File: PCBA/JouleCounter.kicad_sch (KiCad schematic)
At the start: 0 parts

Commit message: Scratching out schematic
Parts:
- added J? (x2): USB_C_Receptacle_USB2.0, symbol Connector:USB_C_Receptacle_USB2.0
- added R?: ?, symbol Device:R_Shunt
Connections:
- new net: J?.A4 (VBUS), J?.A9 (VBUS), J?.B4 (VBUS), J?.B9 (VBUS), R?.4
- new net: J?.A8 (SBU1), J?.A8 (SBU1)
- new net: J?.B8 (SBU2), J?.B8 (SBU2)
- new net CC1: J?.A5 (CC1), J?.A5 (CC1)
- new net CC2: J?.B5 (CC2), J?.B5 (CC2)
- new net GND: J?.A1 (GND), J?.A1 (GND), J?.A12 (GND), J?.A12 (GND), J?.B1 (GND), J?.B1 (GND), J?.B12 (GND), J?.B12 (GND), J?.S1 (SHIELD), J?.S1 (SHIELD)
- new net USB_D+: J?.A6 (D+), J?.A6 (D+), J?.B6 (D+), J?.B6 (D+)
- new net USB_D-: J?.A7 (D-), J?.A7 (D-), J?.B7 (D-), J?.B7 (D-)
- new net VBUS: J?.A4 (VBUS), J?.A9 (VBUS), J?.B4 (VBUS), J?.B9 (VBUS), R?.1
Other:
- removed sheet PineNut-12S
- added sheet FUSB302 (fusb302.kicad_sch)
- added sheet Flash (Flash.kicad_sch)
- added sheet Main MCU (mcu.kicad_sch)
- note added: "Pull high for prog"
- note added: "https://raw.githubusercontent.com/riscv/riscv-debug-spec/master/riscv-debug-stable.pdf Page 92"

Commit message: Input/output jacks
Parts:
- removed J? (x2): USB_C_Receptacle_USB2.0, symbol Connector:USB_C_Receptacle_USB2.0
- removed R?: ?, symbol Device:R_Shunt
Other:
- added sheet Measurement ports (measurement.kicad_sch)

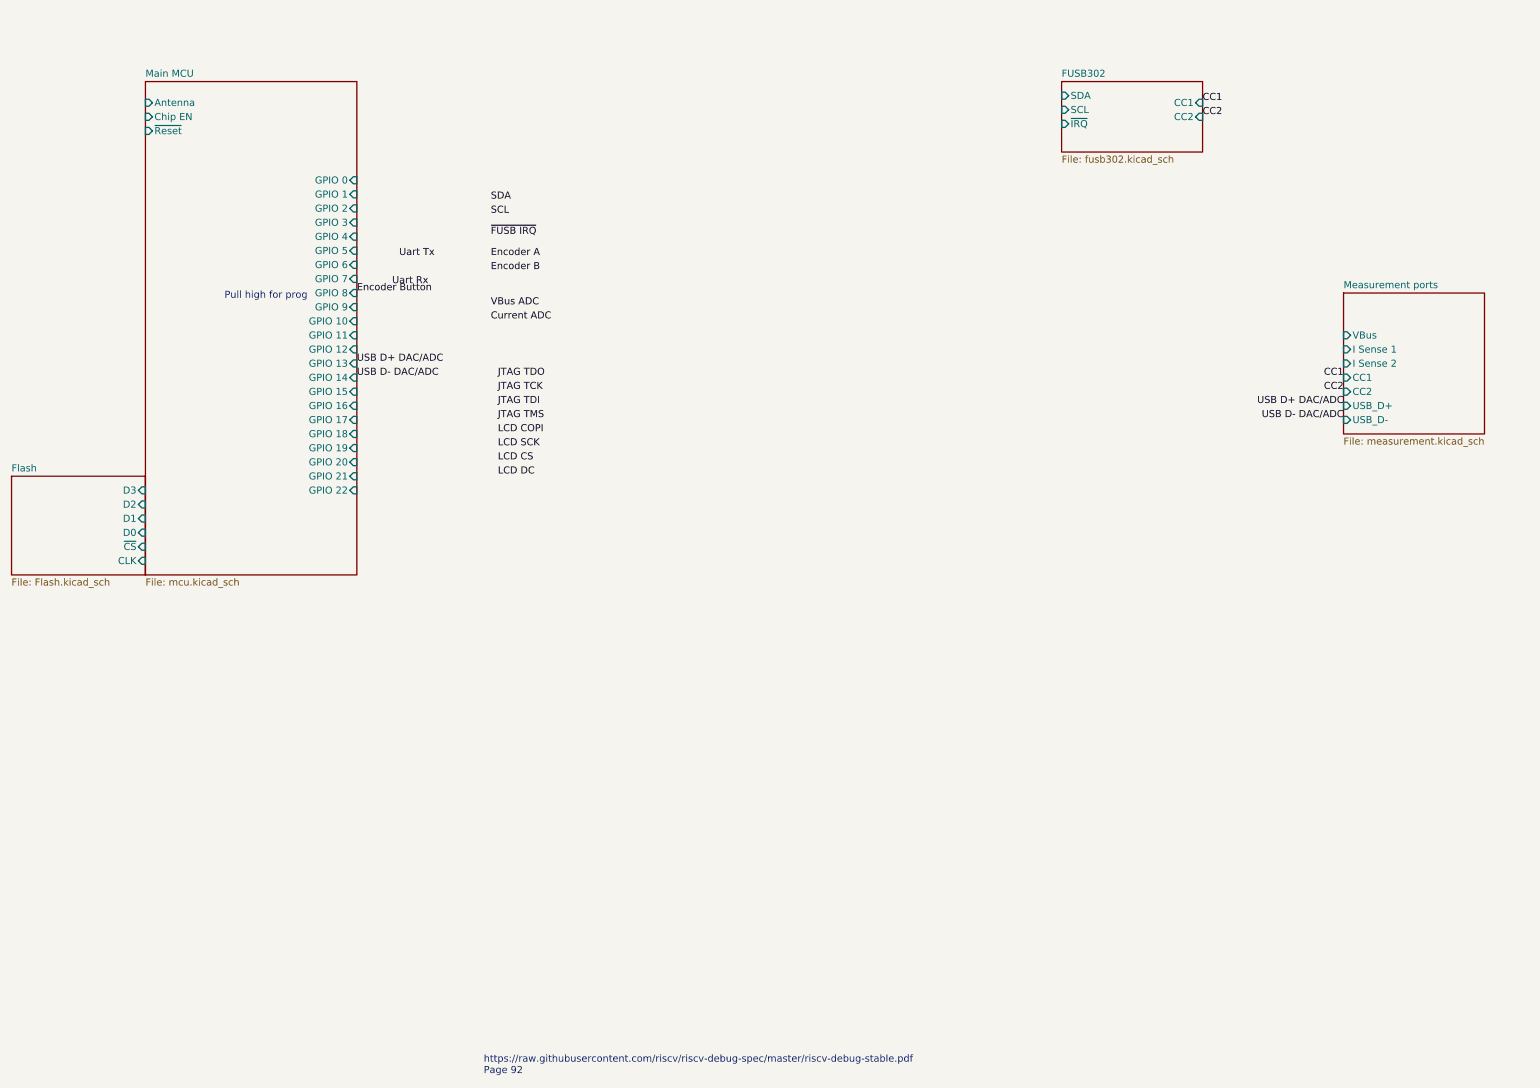
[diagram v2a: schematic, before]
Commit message: Programming uart added
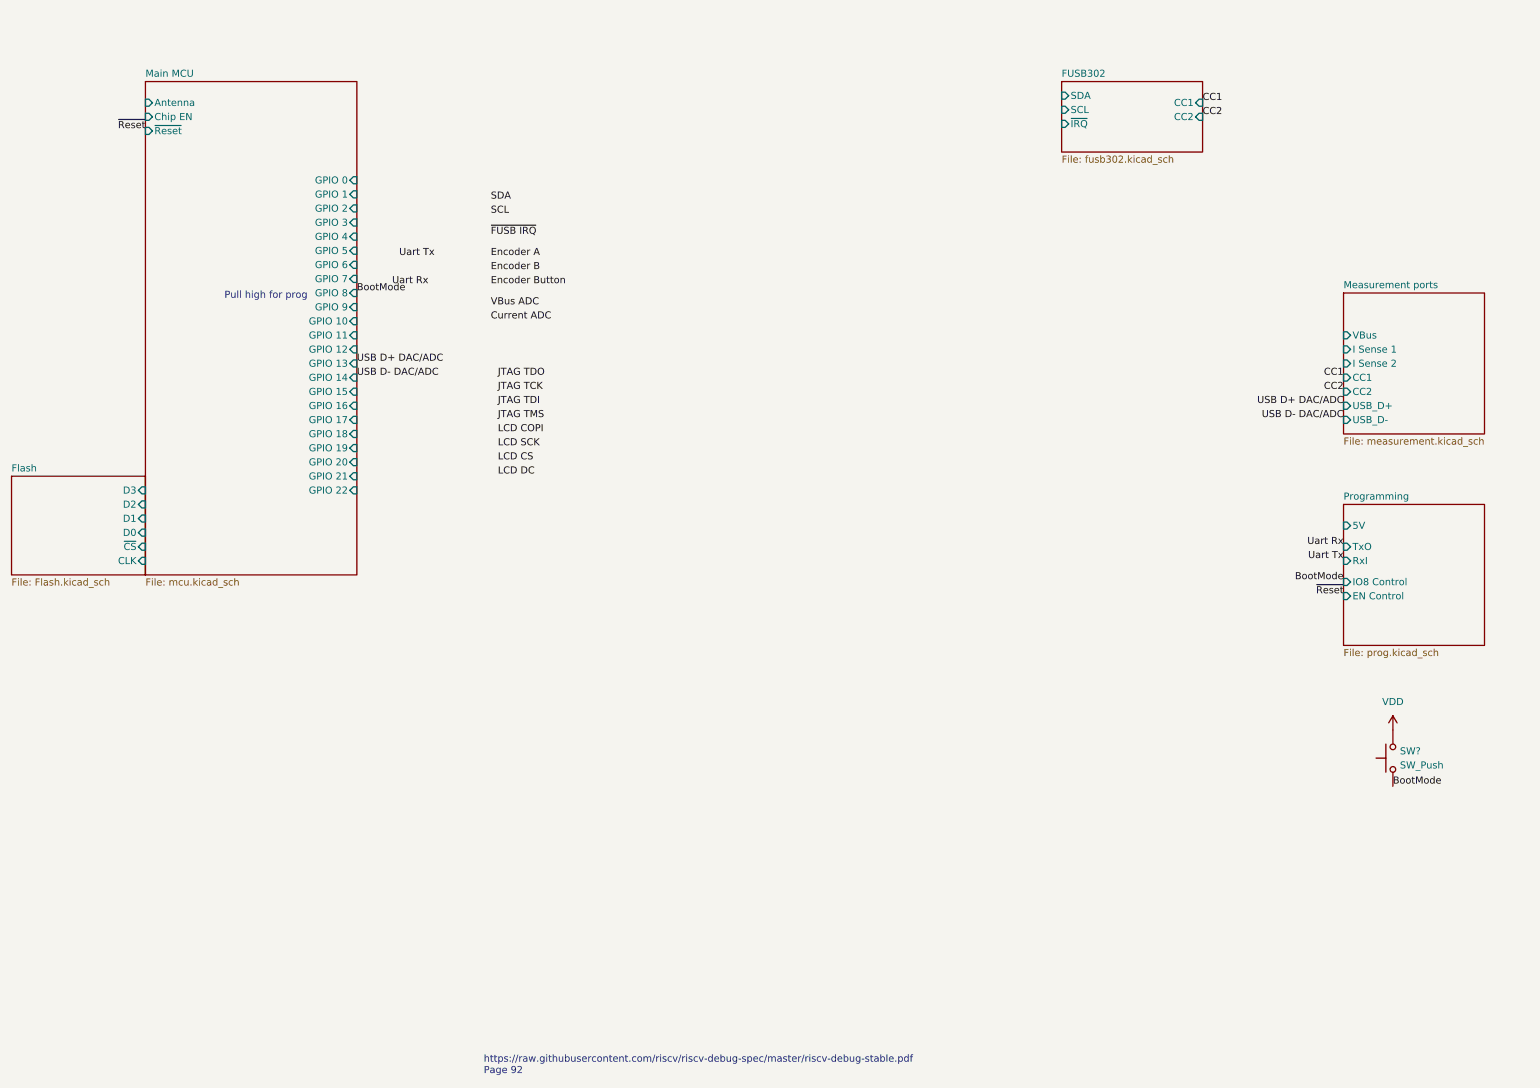
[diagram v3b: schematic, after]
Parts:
- added SW?: SW_Push, symbol Switch:SW_Push
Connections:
- new net BootMode: SW?.1
- new net VDD: SW?.2
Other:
- added sheet Programming (prog.kicad_sch)
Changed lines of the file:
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@@
     (effects (font (size 1.27 1.27)) (justify left bottom))
+  )
+  (label "Uart Rx" (at 254 109.22 180)
+    (effects (font (size 1.27 1.27)) (justify right bottom))
   )
   (label "CC1" (at 228.6 29.21 0)
@@
     (effects (font (size 1.27 1.27)) (justify left bottom))
   )
+  (label "BootMode" (at 262.89 152.4 0)
+    (effects (font (size 1.27 1.27)) (justify left bottom))
+  )
   (label "USB D+ DAC{slash}ADC" (at 254 83.82 180)
     (effects (font (size 1.27 1.27)) (justify right bottom))
   )
+  (label "BootMode" (at 76.2 63.5 0)
+    (effects (font (size 1.27 1.27)) (justify left bottom))
+  )
   (label "JTAG TMS" (at 101.6 86.36 0)
     (effects (font (size 1.27 1.27)) (justify left bottom))
@@
     (effects (font (size 1.27 1.27)) (justify left bottom))
   )
-  (label "Encoder Button" (at 76.2 63.5 0)
+  (label "Encoder Button" (at 100.33 62.23 0)
     (effects (font (size 1.27 1.27)) (justify left bottom))
   )
@@
     (effects (font (size 1.27 1.27)) (justify right bottom))
   )
+  (label "~{Reset}" (at 38.1 34.29 180)
+    (effects (font (size 1.27 1.27)) (justify right bottom))
+  )
   (label "Current ADC" (at 100.33 68.58 0)
     (effects (font (size 1.27 1.27)) (justify left bottom))
@@
     (effects (font (size 1.27 1.27)) (justify left bottom))
   )
+  (label "~{Reset}" (at 254 118.11 180)
+    (effects (font (size 1.27 1.27)) (justify right bottom))
+  )
   (label "SCL" (at 100.33 49.53 0)
     (effects (font (size 1.27 1.27)) (justify left bottom))
   )
+  (label "Uart Tx" (at 254 111.76 180)
+    (effects (font (size 1.27 1.27)) (justify right bottom))
+  )
+  (label "BootMode" (at 254 115.57 180)
+    (effects (font (size 1.27 1.27)) (justify right bottom))
+  )
   (label "JTAG TDO" (at 101.6 78.74 0)
     (effects (font (size 1.27 1.27)) (justify left bottom))
@@
   (label "Encoder A" (at 100.33 57.15 0)
     (effects (font (size 1.27 1.27)) (justify left bottom))
+  )
+  (symbol (lib_id "power:VDD") (at 262.89 142.24 0) (unit 1)
+    (in_bom yes) (on_board yes) (fields_autoplaced)
+    (property "Reference" "#PWR?" (id 0) (at 262.89 146.05 0)
+      (effects (font (size 1.27 1.27)) hide)
+    )
+    (property "Value" "VDD" (id 1) (at 262.89 137.16 0))
+    (property "Footprint" "" (id 2) (at 262.89 142.24 0)
+      (effects (font (size 1.27 1.27)) hide)
+    )
+    (property "Datasheet" "" (id 3) (at 262.89 142.24 0)
+      (effects (font (size 1.27 1.27)) hide)
+    )
+    (pin "1")
+  )
+  (symbol (lib_id "Switch:SW_Push") (at 262.89 147.32 90) (unit 1)
+    (in_bom yes) (on_board yes) (fields_autoplaced)
+    (property "Reference" "SW?" (id 0) (at 264.16 146.0499 90)
+      (effects (font (size 1.27 1.27)) (justify right))
+    )
+    (property "Value" "SW_Push" (id 1) (at 264.16 148.5899 90)
+      (effects (font (size 1.27 1.27)) (justify right))
+    )
+    (property "Footprint" "" (id 2) (at 257.81 147.32 0)
+      (effects (font (size 1.27 1.27)) hide)
+    )
+    (property "Datasheet" "~" (id 3) (at 257.81 147.32 0)
+      (effects (font (size 1.27 1.27)) hide)
+    )
+    (pin "1")
+    (pin "2")
   )
   (sheet (at 254 63.5) (size 25.4 25.4) (fields_autoplaced)
@@
     )
     (pin "~{IRQ}" input (at 203.2 33.02 180)
+      (effects (font (size 1.27 1.27)) (justify left))
+    )
+  )
+  (sheet (at 254 101.6) (size 25.4 25.4) (fields_autoplaced)
+    (stroke (width 0.1524) (type solid) (color 0 0 0 0))
+    (fill (color 221 133 0 0.4400))
+    (property "Sheet name" "Programming" (id 0) (at 254 100.8884 0)
+      (effects (font (size 1.27 1.27)) (justify left bottom))
+    )
+    (property "Sheet file" "prog.kicad_sch" (id 1) (at 254 127.5846 0)
+      (effects (font (size 1.27 1.27)) (justify left top))
+    )
+    (pin "5V" input (at 254 105.41 180)
+      (effects (font (size 1.27 1.27)) (justify left))
+    )
+    (pin "TxO" input (at 254 109.22 180)
+      (effects (font (size 1.27 1.27)) (justify left))
+    )
+    (pin "RxI" input (at 254 111.76 180)
+      (effects (font (size 1.27 1.27)) (justify left))
+    )
+    (pin "IO8 Control" input (at 254 115.57 180)
+      (effects (font (size 1.27 1.27)) (justify left))
+    )
+    (pin "EN Control" input (at 254 118.11 180)
       (effects (font (size 1.27 1.27)) (justify left))
     )
@@
     (path "/7bd54514-8f0a-4683-8b19-da3af36c1bff" (page "4"))
     (path "/11e6ad7b-94c7-4abc-98e0-e4b10d097f65" (page "5"))
+    (path "/b0bcfef4-b206-452e-922a-e4174969def9" (page "6"))
   )
   (symbol_instances
@@
       (reference "#PWR0126") (unit 1) (value "VDD") (footprint "")
     )
+    (path "/03b39198-386c-42ec-ac3c-5e52c86fb501"
+      (reference "#PWR?") (unit 1) (value "VDD") (footprint "")
+    )
     (path "/11e6ad7b-94c7-4abc-98e0-e4b10d097f65/1a3f0213-743d-4c90-abd3-c55d0cbfe304"
       (reference "#PWR?") (unit 1) (value "GND") (footprint "")
     )
+    (path "/b0bcfef4-b206-452e-922a-e4174969def9/42d40598-f1c5-4992-939b-06617e7a59a8"
+      (reference "#PWR?") (unit 1) (value "GND") (footprint "")
+    )
+    (path "/b0bcfef4-b206-452e-922a-e4174969def9/4491f562-375c-4b17-af2c-bca5491dc619"
+      (reference "#PWR?") (unit 1) (value "GND") (footprint "")
+    )
     (path "/11e6ad7b-94c7-4abc-98e0-e4b10d097f65/71ab0170-4f26-4c83-a555-73006c324284"
       (reference "#PWR?") (unit 1) (value "GND") (footprint "")
     )
+    (path "/b0bcfef4-b206-452e-922a-e4174969def9/7e9a9ae1-dcfe-49cc-bd9c-cd4b104862e7"
+      (reference "#PWR?") (unit 1) (value "VDD") (footprint "")
+    )
+    (path "/b0bcfef4-b206-452e-922a-e4174969def9/9f3d64f9-7499-418d-a1b7-b157563ccb7a"
+      (reference "#PWR?") (unit 1) (value "GND") (footprint "")
+    )
+    (path "/b0bcfef4-b206-452e-922a-e4174969def9/a8eb7153-7048-46ab-96b7-c4250fc262cc"
+      (reference "#PWR?") (unit 1) (value "VDD") (footprint "")
+    )
     (path "/11e6ad7b-94c7-4abc-98e0-e4b10d097f65/a9a5044a-0486-4799-b3bf-d571aea47b0e"
+      (reference "#PWR?") (unit 1) (value "GND") (footprint "")
+    )
+    (path "/b0bcfef4-b206-452e-922a-e4174969def9/e988f392-1a6f-4da7-84c4-2e8322b85075"
       (reference "#PWR?") (unit 1) (value "GND") (footprint "")
     )
@@
       (reference "J?") (unit 1) (value "Jack-DC") (footprint "")
     )
+    (path "/b0bcfef4-b206-452e-922a-e4174969def9/fd8423c4-1899-4f45-bc5c-5ade0ca4f7dd"
+      (reference "J?") (unit 1) (value "USB_C_Receptacle_USB2.0") (footprint "")
+    )
     (path "/4847c8c0-6173-45c5-9b4b-8c9418cb5a91/3110ff89-db45-4c2b-ae20-9f45ed5b62f3"
       (reference "L201") (unit 1) (value "2.2uH") (footprint "")
@@
       (reference "R201") (unit 1) (value "10k") (footprint "Resistor_SMD:R_0603_1608Metric")
     )
+    (path "/4847c8c0-6173-45c5-9b4b-8c9418cb5a91/39abf5a4-a61a-44ed-9b3a-247098f2a58b"
+      (reference "R?") (unit 1) (value "10k") (footprint "Resistor_SMD:R_0603_1608Metric")
+    )
+    (path "/b0bcfef4-b206-452e-922a-e4174969def9/5a1caade-c200-4269-a681-364a990f31cb"
+      (reference "R?") (unit 1) (value "5.1k") (footprint "")
+    )
     (path "/11e6ad7b-94c7-4abc-98e0-e4b10d097f65/b3b71854-67cf-4268-af94-58f58f9488b0"
       (reference "R?") (unit 1) (value "?") (footprint "")
     )
+    (path "/b0bcfef4-b206-452e-922a-e4174969def9/d6fe3a78-f56d-4514-9a84-6d78d454e767"
+      (reference "R?") (unit 1) (value "5.1k") (footprint "")
+    )
+    (path "/4847c8c0-6173-45c5-9b4b-8c9418cb5a91/f85b8bad-256f-47fa-862d-eebf043e510d"
+      (reference "R?") (unit 1) (value "10k") (footprint "Resistor_SMD:R_0603_1608Metric")
+    )
+    (path "/d84dd542-2064-402c-89ca-733f0c5aa49f"
+      (reference "SW?") (unit 1) (value "SW_Push") (footprint "")
+    )
     (path "/4847c8c0-6173-45c5-9b4b-8c9418cb5a91/93a38881-2e11-46cb-83bc-4368921a90cd"
       (reference "U201") (unit 1) (value "BL604") (footprint "Package_DFN_QFN:QFN-40-1EP_5x5mm_P0.4mm_EP3.6x3.6mm")
@@
       (reference "U401") (unit 1) (value "FUSB302B") (footprint "Package_DFN_QFN:WQFN-14-1EP_2.5x2.5mm_P0.5mm_EP1.45x1.45mm")
     )
+    (path "/b0bcfef4-b206-452e-922a-e4174969def9/cf117e68-fb24-4a6a-9654-ebd962bcdc90"
+      (reference "U?") (unit 1) (value "CH340E") (footprint "Package_SO:MSOP-10_3x3mm_P0.5mm")
+    )
     (path "/4847c8c0-6173-45c5-9b4b-8c9418cb5a91/c5a59dc7-2bb1-40d5-9012-f726395f3506"

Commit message: ADC readings
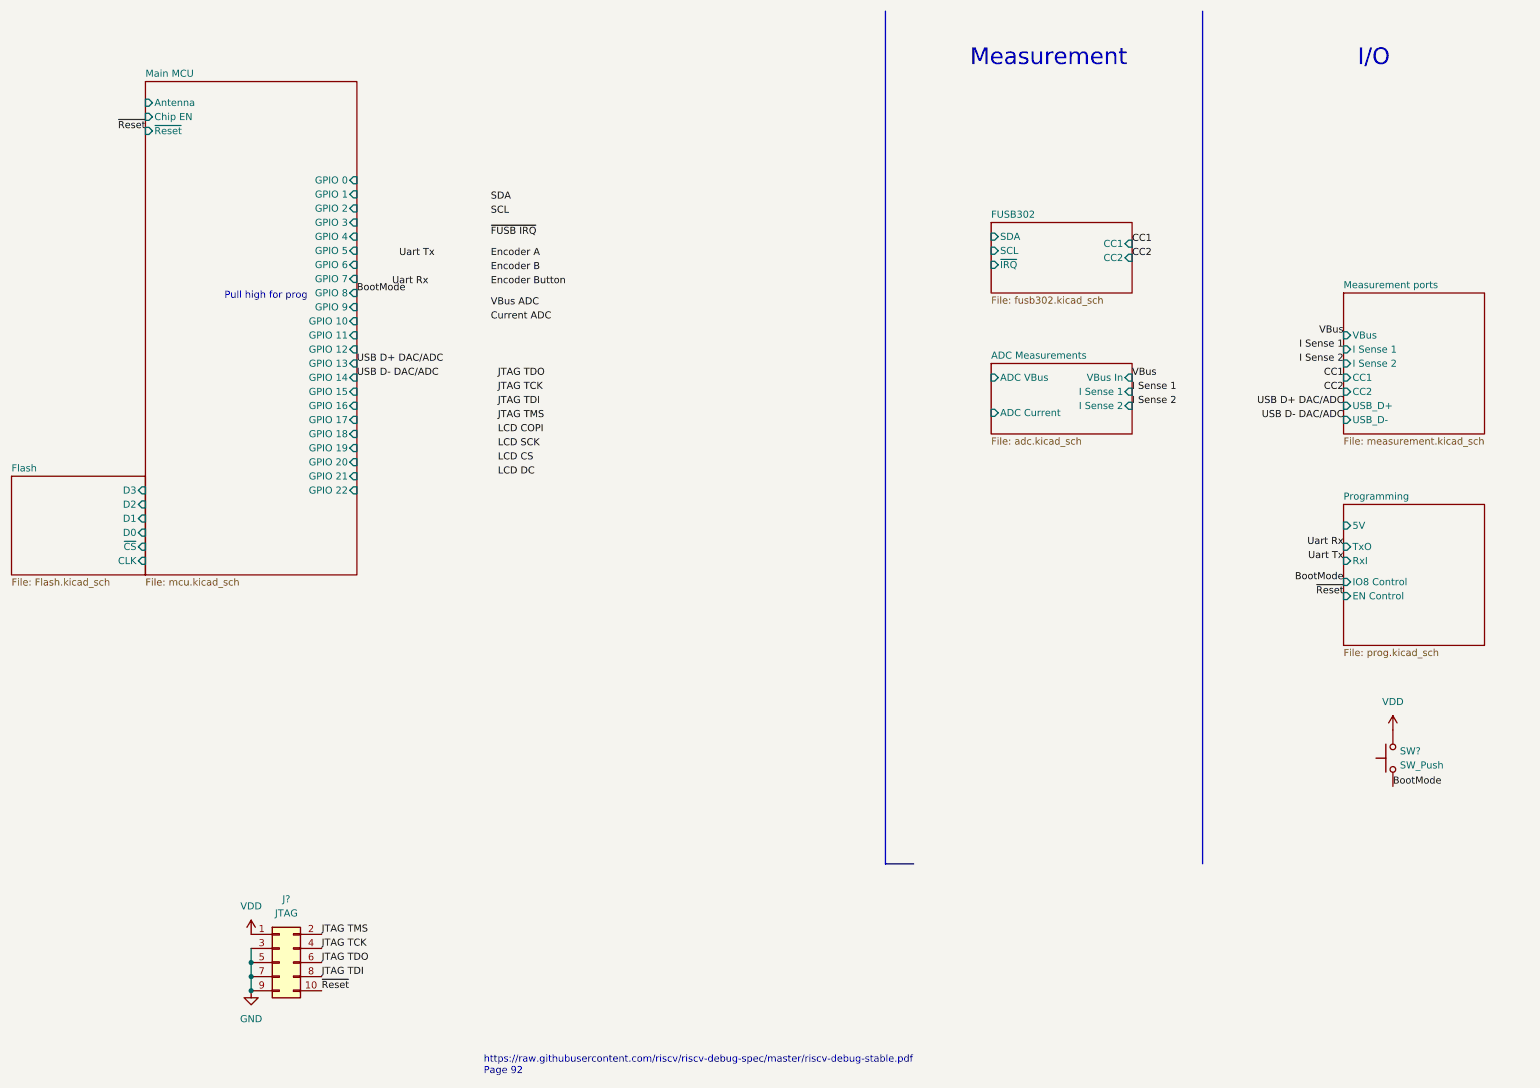
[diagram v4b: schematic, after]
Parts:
- added J?: JTAG, symbol Connector_Generic:Conn_02x05_Odd_Even
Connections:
- net JTAG TCK: now also J?.4 (Pin_4)
- net JTAG TDI: now also J?.8 (Pin_8)
- net JTAG TDO: now also J?.6 (Pin_6)
- net JTAG TMS: now also J?.2 (Pin_2)
- net VDD: now also J?.1 (Pin_1)
- net ~{Reset}: now also J?.10 (Pin_10)
- new net GND: J?.3 (Pin_3), J?.5 (Pin_5), J?.7 (Pin_7), J?.9 (Pin_9)
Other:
- added sheet ADC Measurements (adc.kicad_sch)
- note added: "I/O"
- note added: "Measurement"
